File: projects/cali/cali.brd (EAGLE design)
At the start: 100 x 80 mm, 25 parts, among them Q3 IRF540, T1 BC547, T2 BC547, T3 BC547

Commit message: Board v1.0
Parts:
- removed Q3: IRF540, transistor-power:TO220BV
- removed R15, R17: 10k, rcl:0207/10
- removed R16: 1k, rcl:0207/10
- removed R18: 10, rcl:0207/10
- added D1: BAS316, nxp_60:SOD323(F)
- added R11: 10k, rcl:R1206
- added T4: IRLML2502, we-transistor:SOT23
- added U$4: FINDER-36.11, relay2:FINDER-36.11
- added X2: (no value), con-ptr500:AK500/4
- R1: value 0 -> 100; device rcl:0207/10 -> rcl:R1206
- R10: value 10k -> 1k; device rcl:0207/10 -> rcl:R1206
- R12: value 4k7 -> 1k; device rcl:0207/10 -> rcl:R1206
- R13: value 1k -> 0; device rcl:0207/10 -> rcl:R1206
- R14: value 10k -> 2k; device rcl:0207/10 -> rcl:R1206
- R2, R6: value 1k -> 100; device rcl:0207/10 -> rcl:R1206
- R3, R4, R5, R7, R8: device rcl:0207/10 -> rcl:R1206
- R9: value 1k -> 10k; device rcl:0207/10 -> rcl:R1206
- T1, T2: value BC547 -> IRLML2502; device transistor:TO92 -> we-transistor:SOT23
- T3: value BC547 -> 2N7002E; device transistor:TO92 -> nxp_60:SOT23
- moved X1 73.8 mm to (45.7, 81.3), turned to 180 degrees
- moved R5 59.1 mm to (66.0, 55.9), turned to 0 degrees
- moved R8 51.8 mm to (63.5, 22.9), turned to 0 degrees
- moved R4 49.8 mm to (53.3, 17.8), turned to 270 degrees
- moved T1 44.9 mm to (15.2, 17.8), turned to 0 degrees
- moved R13 44.8 mm to (58.4, 53.3), turned to 0 degrees
- moved R3 39.5 mm to (35.6, 55.9), turned to 0 degrees
- moved R14 35.5 mm to (38.1, 61.0)
- moved R10 33.8 mm to (48.3, 58.4), turned to 0 degrees
- moved T3 33.1 mm to (63.5, 15.2), turned to 0 degrees
- moved R2 32.2 mm to (45.7, 48.3), turned to 0 degrees
- moved R9 31.5 mm to (15.2, 53.3)
- moved R6 22.9 mm to (12.7, 66.0)
- moved T2 18.1 mm to (40.6, 68.6)
- moved R12 16.8 mm to (66.0, 35.6), turned to 0 degrees
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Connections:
- removed net 5V0@1: U$2.2
- removed net N$16: Q3.G, R18.2
- removed net N$17: Q3.D, X1.11
- removed net N$18: R12.1, U$2.37, X1.7
- removed net N$20: U$2.40, X1.5
- removed net N$21: U$2.38, X1.6
- removed net N$22: R9.2, T3.2
- removed net N$23: R10.1, T3.3, X1.8
- new net ADC0: U$1.7
- new net ADC1: R7.1, R8.1, U$1.8
- new net ADC2: R10.1, R9.1, U$1.9
- new net ADC3: R11.1, R12.1, U$1.10
- new net ADC4: R13.1, R14.1
- new net GPIO12: R6.1, U$2.32
- new net GPIO16: R1.1, U$2.36
- new net GPIO20: T2.2, U$2.38
- new net GPIO21: R5.1, T3.3, U$2.40
- new net GPIO26: U$2.37, X1.5
- net +12V: now also D1.1, R3.2, R4.2, U$4.A1, X2.4; no longer R10.2, R17.2, X1.10
- net +3V3: now also R2.2, R5.2, X2.3; no longer R12.2, R15.2, X1.9
- net GND: now also R10.2, R12.2, R14.2, R8.2, T1.2, T4.2, U$2.6, X2.1, X2.2; no longer Q3.S, R13.1, R4.1, R6.1, R8.1, T1.1, T2.1, T3.1
- net GPIO19: no longer R9.1
- net N$1: now also D1.2, T4.3, U$4.A2; no longer R1.1, X1.1
- net N$10: now also R2.1, T2.1; no longer R14.1, T1.2
- net N$11: now also R3.1, T2.3, X1.10; no longer R14.2, X1.12
- net N$12: now also R4.1, T3.1; no longer R15.1, T1.3, U$2.36
- net N$13: now also T3.2, X1.9; no longer R16.2, T2.2
- net N$14: now also R11.2, X1.3; no longer R16.1, U$2.32
- net N$15: now also R13.2, X1.4; no longer R17.1, R18.1, T2.3
- net N$2: now also T1.3, X1.11; no longer R3.1, X1.2
- net N$3: now also U$4.NO, X1.8; no longer R5.1, X1.3
- net N$4: now also R6.2, T4.1; no longer R7.1, X1.4
- net N$5: now also U$4.COM, X1.6; no longer R1.2, R2.2, U$1.10
- net N$6: now also R1.2, T1.1; no longer R3.2, R4.2, U$1.9
- net N$7: now also U$4.NC, X1.7; no longer R13.2, R2.1
- net N$8: now also X1.1; no longer R8.2, U$1.7
- net N$9: now also R9.2, X1.2; no longer R5.2, R6.2, U$1.8
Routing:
- net +3V3: track 207.9 -> 0.00 mm
- net GND: track 197.3 -> 0.00 mm
- net N$5: track 131.2 -> 0.00 mm
- net N$6: track 117.3 -> 0.00 mm
- net N$9: track 106.1 -> 0.00 mm
- net N$8: track 95.4 -> 0.00 mm
- net SCL: track 92.7 -> 0.00 mm
- net SDA: track 87.5 -> 0.00 mm
- net N$17: track 53.0 -> 0.00 mm
- net N$12: track 45.7 -> 0.00 mm
- net N$18: track 43.6 -> 0.00 mm
- net N$11: track 41.8 -> 0.00 mm
- net N$23: track 40.0 -> 0.00 mm
- net N$15: track 35.7 -> 0.00 mm
- net +12V: track 33.9 -> 0.00 mm
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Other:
- board size 100 x 80 mm -> 90 x 90 mm
- board text added: "12V"
- board text added: "3V3"
- board text added: "GND"

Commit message: Caliboard 1.0 routing done
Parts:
- added R15: 0, rcl:R1206
- added X3, X4: (no value), con-ptr500:AK500/4
- X1: device con-ptr500:AK500/12 -> con-ptr500:AK500/4
- moved U$3 82.8 mm to (23.1, 3.43), turned to 90 degrees
- moved X1 73.6 mm to (85.1, 19.1), turned to 90 degrees
- moved U$1 72.4 mm to (10.2, 45.7)
- moved R1 69.1 mm to (72.4, 41.9), flipped to the bottom, turned to 270 degrees
- moved R8 59.7 mm to (8.89, 47.0), turned to 180 degrees
- moved T1 59.5 mm to (72.4, 34.3), flipped to the bottom, turned to 270 degrees
- moved R12 59.1 mm to (8.89, 50.8), flipped to the bottom
- moved R11 57.1 mm to (8.89, 54.6), flipped to the bottom, turned to 0 degrees
- moved U$2 50.6 mm to (20.8, 30.7), turned to 0 degrees
- moved R3 46.2 mm to (72.4, 27.9), flipped to the bottom, turned to 270 degrees
- moved R5 37.0 mm to (31.8, 41.9), turned to 90 degrees
- moved R13 35.6 mm to (22.9, 53.3)
- moved D1 34.7 mm to (30.5, 19.1), flipped to the bottom, turned to 90 degrees
- moved R6 34.1 mm to (36.8, 41.9), flipped to the bottom, turned to 270 degrees
- moved T2 30.5 mm to (49.5, 39.4), flipped to the bottom, turned to 270 degrees
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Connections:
- removed net ADC4: R13.1, R14.1
- removed net N$14: R11.2, X1.3
- removed net N$15: R13.2, X1.4
- new net I_SOL: R13.2, X3.4
- new net V_SOL: R7.2, X3.1
- new net V_START: R11.2, X3.3
- net ADC0: now also R7.1, R8.1
- net ADC1: now also R10.1, R9.1; no longer R7.1, R8.1
- net ADC2: now also R11.1, R12.1; no longer R10.1, R9.1
- net ADC3: now also R13.1, R14.1; no longer R11.1, R12.1
- net GPIO19: now also T2.2
- net GPIO20: no longer T2.2
- net GPIO26: now also X4.4; no longer X1.5
- net N$11: now also X1.3; no longer X1.10
- net N$13: now also R15.1, R9.2; no longer T3.2, X1.9
- net N$2: now also X1.4; no longer X1.11
- net N$3: now also X4.3; no longer X1.8
- net N$5: now also X4.2; no longer X1.6
- net N$7: now also X4.1; no longer X1.7
- net N$8: now also T3.2, X1.2; no longer R7.2, X1.1
- net N$9: now also R15.2, X3.2; no longer R9.2, X1.2
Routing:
- net +3V3: track 0.00 -> 145.4 mm
- net I_SOL: track 0.00 -> 118.8 mm
- net +12V: track 0.00 -> 91.6 mm
- net GPIO21: track 0.00 -> 86.5 mm
- net V_START: track 0.00 -> 82.0 mm
- net SCL: track 0.00 -> 57.0 mm
- net SDA: track 0.00 -> 53.7 mm
- net V_SOL: track 0.00 -> 53.5 mm
- net N$11: track 0.00 -> 42.7 mm
- net N$9: track 0.00 -> 41.4 mm
- net GPIO12: track 0.00 -> 39.1 mm
- net GPIO26: track 0.00 -> 38.9 mm
- net GPIO19: track 0.00 -> 28.4 mm
- net N$1: track 0.00 -> 27.6 mm
- net N$5: track 0.00 -> 27.5 mm
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- added copper zone on layer 1, net GND
- added copper zone on layer 16, net GND
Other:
- board size 90 x 90 mm -> 89.8 x 61.9 mm
- board text added: "CHGI"
- board text added: "CHGO"
- board text added: "COM"
- board text added: "Caliboard 1.0"
- board text added: "FAN"
- board text added: "GPIO26"
- board text added: "ISOL"
- board text added: "NC"
- board text added: "NO"
- board text added: "VBAT"
- board text added: "VSOL"
- board text added: "VSTART"

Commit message: Caliboard 1.0, avoid cutting bottom layer ground plane
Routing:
- net GPIO12: track 39.1 -> 42.7 mm
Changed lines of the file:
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@@
 <contactref element="U$2" pad="32"/>
 <contactref element="R6" pad="1"/>
-<wire x1="36.83" y1="43.332" x2="39.218" y2="45.72" width="0.254" layer="16"/>
-<wire x1="58.42" y1="45.72" x2="66.04" y2="53.34" width="0.254" layer="16"/>
-<wire x1="66.04" y1="53.34" x2="66.04" y2="57.15" width="0.254" layer="16"/>
-<wire x1="66.04" y1="57.15" x2="67.31" y2="58.42" width="0.254" layer="16"/>
+<wire x1="67.31" y1="58.42" x2="66.04" y2="57.15" width="0.254" layer="16"/>
 <wire x1="67.31" y1="58.42" x2="67.31" y2="58.492" width="0.254" layer="16"/>
 <wire x1="67.31" y1="58.492" x2="67.298" y2="58.504" width="0.254" layer="16"/>
-<wire x1="39.218" y1="45.72" x2="58.42" y2="45.72" width="0.254" layer="16"/>
+<wire x1="66.04" y1="57.15" x2="40.64" y2="57.15" width="0.254" layer="16"/>
+<wire x1="40.64" y1="57.15" x2="40.5264" y2="57.0364" width="0.254" layer="16"/>
+<wire x1="40.5264" y1="57.0364" x2="40.5264" y2="47.0284" width="0.254" layer="16"/>
+<wire x1="40.5264" y1="47.0284" x2="36.83" y2="43.332" width="0.254" layer="16"/>
 </signal>
 <signal name="GPIO26">

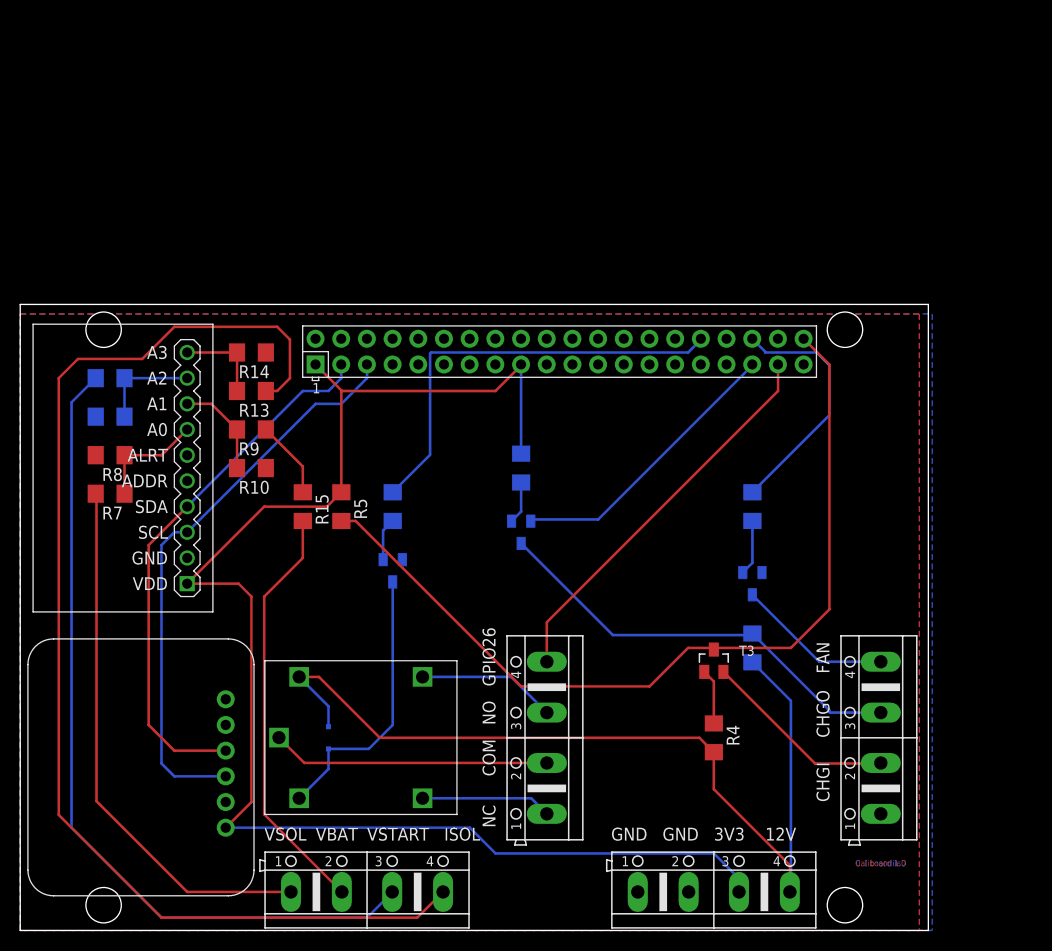
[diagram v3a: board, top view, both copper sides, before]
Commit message: Caliboard v1.1
- Change GPIOs to use GPIO of first row only
- Modify level shifter to sustain 12V
- Change GPIO for PWM
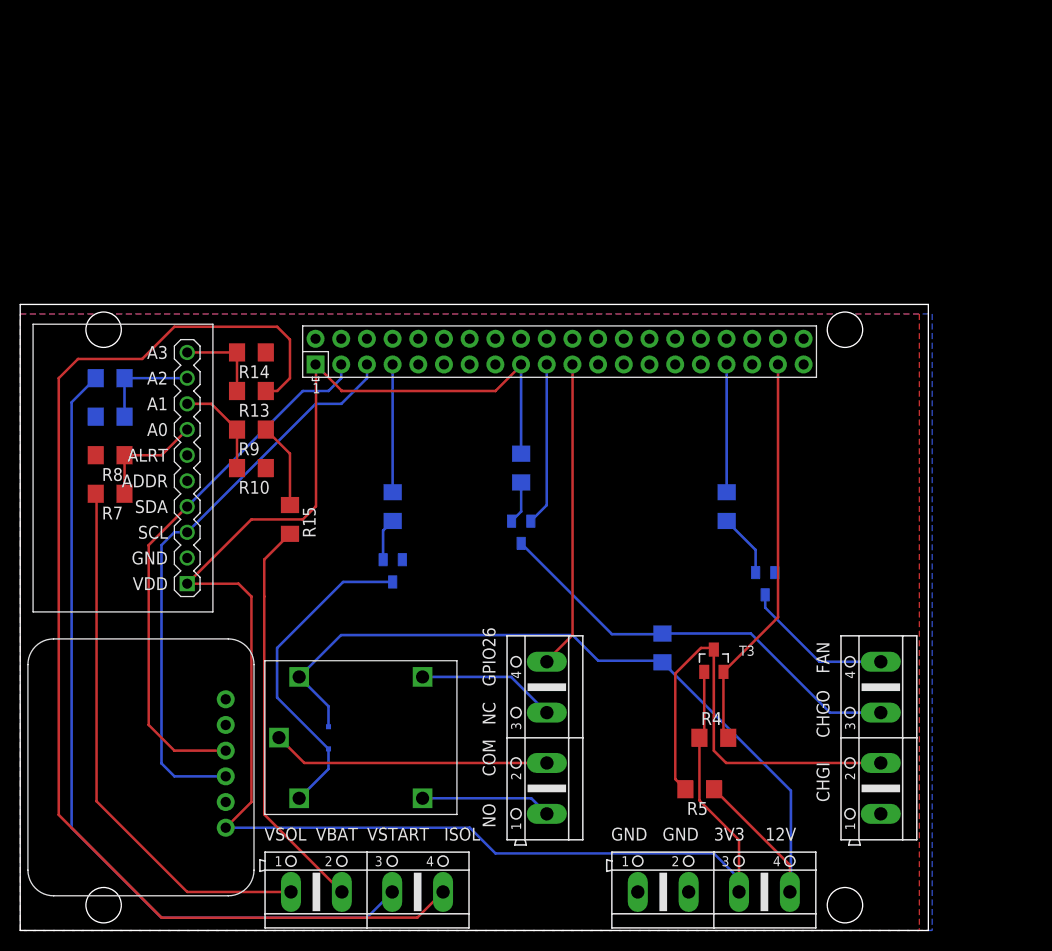
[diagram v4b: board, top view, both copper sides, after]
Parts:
- moved R5 45.1 mm to (67.2, 14.0), turned to 0 degrees
- moved R3 8.89 mm to (63.5, 27.9)
- moved R1 2.54 mm to (69.8, 41.9)
- moved R15 1.80 mm to (26.7, 40.6)
- moved T1 1.27 mm to (73.7, 34.3)
- turned R4 to 0 degrees
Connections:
- removed net N$12: R4.1, T3.1
- removed net N$8: T3.2, X1.2
- new net CHGI: R5.1, T3.3, X1.2
- new net GPIO10: T2.2, U$2.19
- new net GPIO13: R1.1, U$2.33
- new net GPIO4: R6.1, U$2.7
- new net GPIO9: U$2.21, X4.4
- net +12V: now also R5.2; no longer R4.2
- net +3V3: now also R4.1, T3.1; no longer R5.2
- net GND: now also U$2.14, U$2.20, U$2.25, U$2.30, U$2.34, U$2.9
- net GPIO12: no longer R6.1
- net GPIO16: no longer R1.1
- net GPIO19: no longer T2.2
- net GPIO21: no longer R5.1, T3.3
- net GPIO26: now also R4.2, T3.2; no longer X4.4
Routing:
- net GPIO21: track 86.5 -> 0.00 mm
- net CHGI: track 0.00 -> 43.8 mm
- net GPIO12: track 42.7 -> 0.00 mm
- net GPIO9: track 0.00 -> 30.5 mm
- net GPIO19: track 28.4 -> 0.00 mm
- net GPIO16: track 24.5 -> 0.00 mm
- net +3V3: track 145.4 -> 169.8 mm
- net N$8: track 19.3 -> 0.00 mm
- net GPIO10: track 0.00 -> 16.1 mm
- net GPIO4: track 0.00 -> 12.6 mm
- net GPIO13: track 0.00 -> 12.6 mm
- net N$12: track 5.49 -> 0.00 mm
- net +12V: track 91.6 -> 86.1 mm
- net N$1: track 27.6 -> 32.3 mm
- net N$9: track 41.4 -> 39.6 mm
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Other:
- board text added: "Caliboard 1.1 (c) Christian Eisendle"
- board text removed: "Caliboard 1.0"
